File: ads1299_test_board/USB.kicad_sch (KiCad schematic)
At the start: 4 parts, among them P1 USB_C_Plug_USB2.0, U4 TPD2EUSB30, U5 TPD2EUSB30

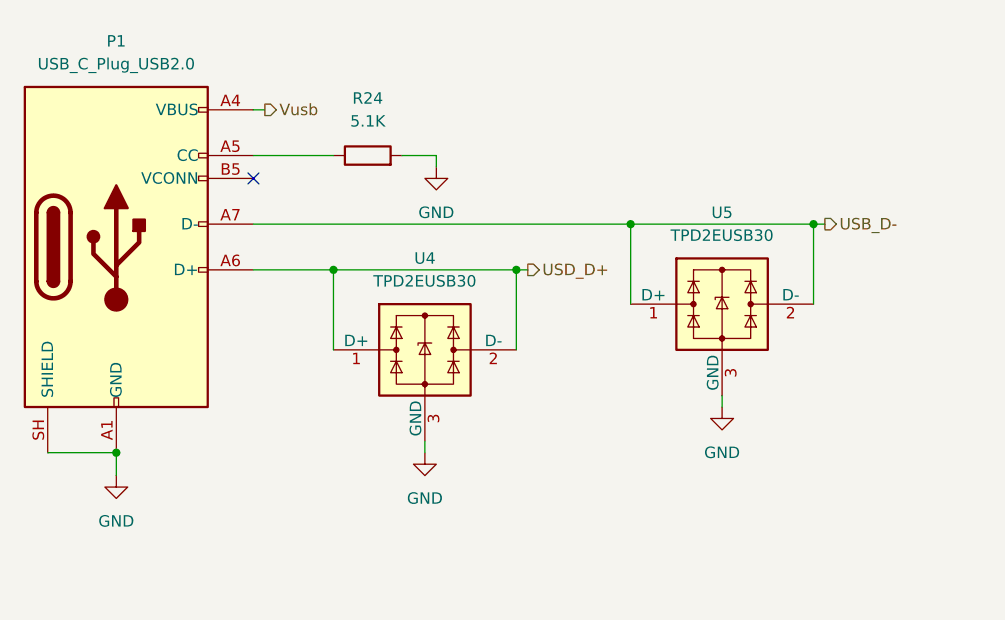
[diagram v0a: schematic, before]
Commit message: usb charge and power circuit switch
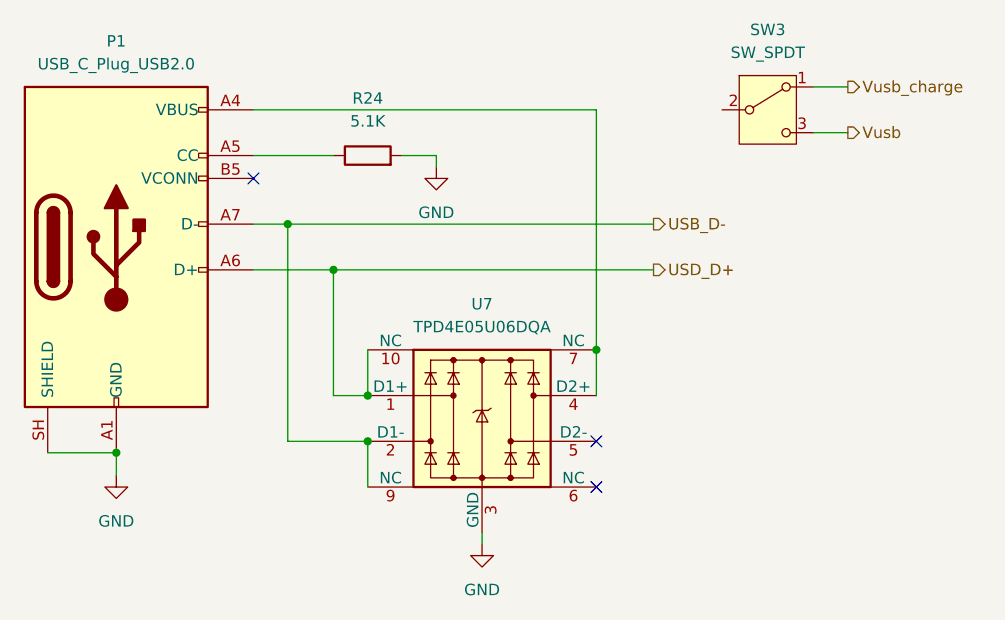
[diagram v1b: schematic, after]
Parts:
- removed U4, U5: TPD2EUSB30, Package_TO_SOT_SMD:Texas_DRT-3, symbol Power_Protection:TPD2EUSB30
- added SW3: SW_SPDT, symbol Switch:SW_SPDT
- added U7: TPD4E05U06DQA, Package_SON:USON-10_2.5x1.0mm_P0.5mm, symbol Power_Protection:TPD4E05U06DQA
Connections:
- net GND: now also U7.3 (GND), U7.8 (GND)
- net USB_D-: now also U7.2 (D1-), U7.9 (NC)
- net USD_D+: now also U7.1 (D1+), U7.10 (NC)
- net Vusb: now also SW3.3 (C); no longer P1.A4 (VBUS), P1.A9 (VBUS), P1.B4 (VBUS), P1.B9 (VBUS)
- new net: P1.A4 (VBUS), P1.A9 (VBUS), P1.B4 (VBUS), P1.B9 (VBUS), U7.4 (D2+), U7.7 (NC)
- new net Vusb_charge: SW3.1 (A)
- no-connect marks 1 -> 3

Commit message: updates
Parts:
- P1: footprint (none) -> Connector_USB:USB_C_Receptacle_G-Switch_GT-USB-7010ASV
- R24: footprint (none) -> Capacitor_SMD:C_0402_1005Metric_Pad0.74x0.62mm_HandSolder
- SW3: footprint (none) -> Button_Switch_THT:SW_Slide_SPDT_Straight_CK_OS102011MS2Q
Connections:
- net Vbus: now reaches SW3.2 (B)
- net Vbus: now also P1.A4 (VBUS), P1.A9 (VBUS), P1.B4 (VBUS), P1.B9 (VBUS), U7.4 (D2+), U7.7 (NC)
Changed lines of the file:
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@@
+	)
+	(junction
+		(at 160.02 76.2)
+		(diameter 0)
+		(color 0 0 0 0)
 	)
 	(junction
@@
 	(wire
 		(pts
+			(xy 184.15 78.74) (xy 187.96 78.74)
+		)
+		(stroke
+			(width 0)
+			(type default)
+		)
+	)
+	(wire
+		(pts
+			(xy 134.62 102.87) (xy 134.62 107.95)
+		)
+		(stroke
+			(width 0)
+			(type default)
+		)
+	)
+	(wire
+		(pts
+			(xy 147.32 123.19) (xy 147.32 124.46)
+		)
+		(stroke
+			(width 0)
+			(type default)
+		)
+	)
+	(wire
+		(pts
+			(xy 121.92 93.98) (xy 130.81 93.98)
+		)
+		(stroke
+			(width 0)
+			(type default)
+		)
+	)
+	(wire
+		(pts
+			(xy 130.81 107.95) (xy 134.62 107.95)
+		)
+		(stroke
+			(width 0)
+			(type default)
+		)
+	)
+	(wire
+		(pts
+			(xy 160.02 76.2) (xy 173.99 76.2)
+		)
+		(stroke
+			(width 0)
+			(type default)
+		)
+	)
+	(wire
+		(pts
+			(xy 130.81 93.98) (xy 166.37 93.98)
+		)
+		(stroke
+			(width 0)
+			(type default)
+		)
+	)
+	(wire
+		(pts
 			(xy 184.15 73.66) (xy 187.96 73.66)
 		)
@@
 	(wire
 		(pts
-			(xy 134.62 102.87) (xy 134.62 107.95)
-		)
-		(stroke
-			(width 0)
-			(type default)
-		)
-	)
-	(wire
-		(pts
-			(xy 147.32 123.19) (xy 147.32 124.46)
-		)
-		(stroke
-			(width 0)
-			(type default)
-		)
-	)
-	(wire
-		(pts
-			(xy 121.92 93.98) (xy 130.81 93.98)
-		)
-		(stroke
-			(width 0)
-			(type default)
-		)
-	)
-	(wire
-		(pts
-			(xy 184.15 78.74) (xy 187.96 78.74)
-		)
-		(stroke
-			(width 0)
-			(type default)
-		)
-	)
-	(wire
-		(pts
-			(xy 130.81 107.95) (xy 134.62 107.95)
-		)
-		(stroke
-			(width 0)
-			(type default)
-		)
-	)
-	(wire
-		(pts
-			(xy 130.81 93.98) (xy 166.37 93.98)
-		)
-		(stroke
-			(width 0)
-			(type default)
-		)
-	)
-	(wire
-		(pts
 			(xy 130.81 93.98) (xy 130.81 107.95)
 		)
@@
 			(width 0)
 			(type default)
+		)
+	)
+	(label "Vbus"
+		(at 123.19 76.2 0)
+		(effects
+			(font
+				(size 1.27 1.27)
+			)
+			(justify left bottom)
 		)
 	)
@@
 			)
 		)
-		(property "Footprint" ""
+		(property "Footprint" "Capacitor_SMD:C_0402_1005Metric_Pad0.74x0.62mm_HandSolder"
 			(at 134.62 83.058 90)
 			(hide yes)
@@
 			)
 		)
-		(property "Footprint" ""
+		(property "Footprint" "Button_Switch_THT:SW_Slide_SPDT_Straight_CK_OS102011MS2Q"
 			(at 179.07 76.2 0)
 			(hide yes)
@@
 			)
 		)
-		(property "Description" "Switch, single pole double throw"
+		(property "Description" "MFS101D-10-Z"
 			(at 179.07 76.2 0)
 			(hide yes)
@@
 			)
 		)
-		(property "Footprint" ""
+		(property "Footprint" "Connector_USB:USB_C_Receptacle_G-Switch_GT-USB-7010ASV"
 			(at 110.49 91.44 0)
 			(hide yes)
@@
 			)
 		)
-		(property "Description" "USB 2.0-only Type-C Plug connector"
+		(property "Description" "D13-0824-16007"
 			(at 106.68 91.44 0)
 			(hide yes)
